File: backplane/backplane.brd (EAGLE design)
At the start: 177 x 80 mm, 9 parts, among them J1 09232486825, J2 09232486825, J3 09232486825, J4 09232486825, J5 09232486825, J6 09232486825, J7 09232486825, J8 09232486825, J9 TB009-508-04BE

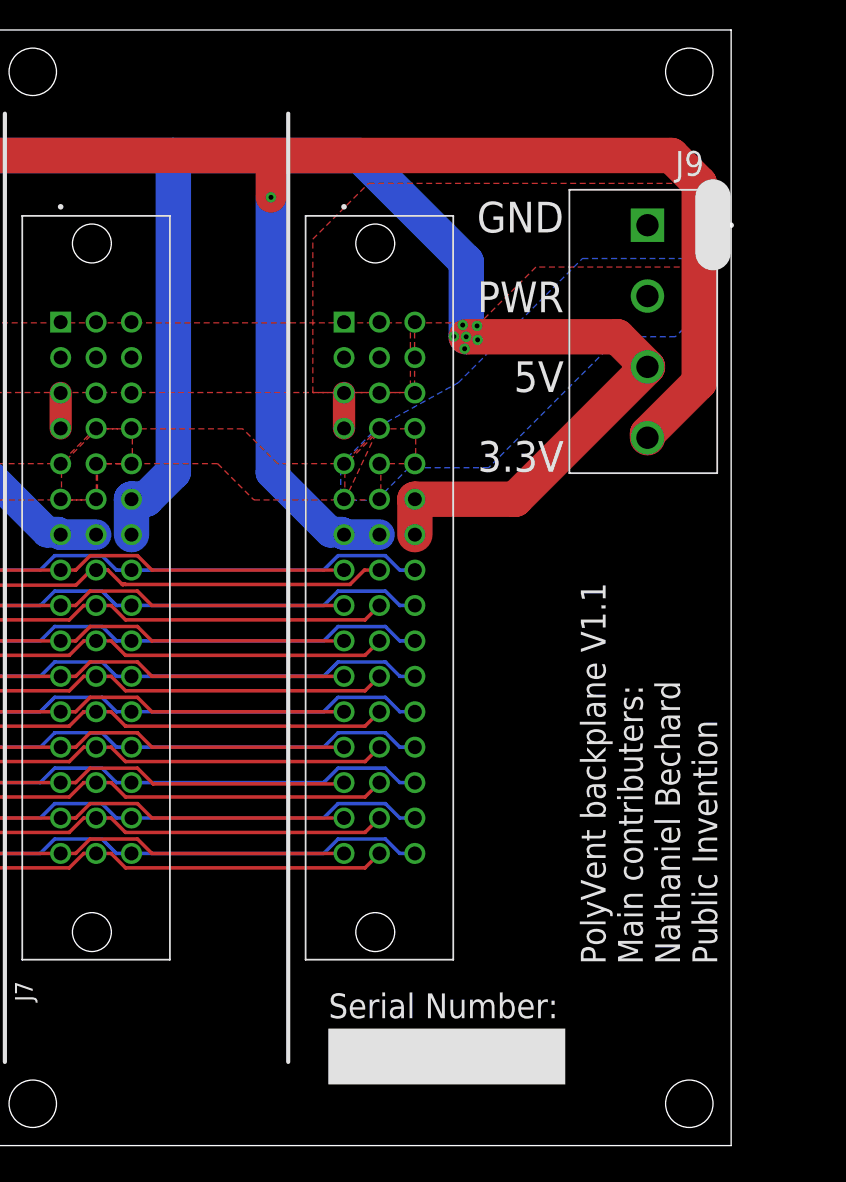
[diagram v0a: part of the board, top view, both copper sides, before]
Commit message: added labeled backplane breakout connector, backplane pcb is done
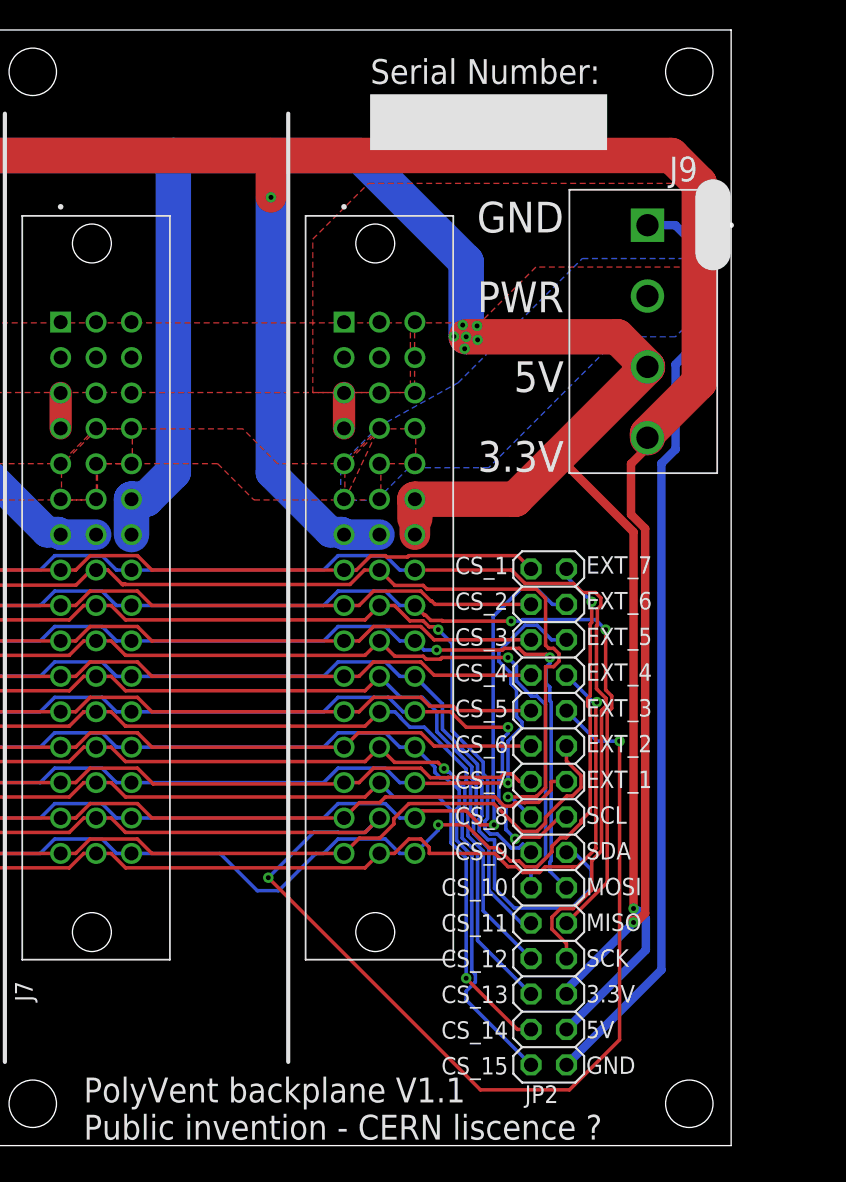
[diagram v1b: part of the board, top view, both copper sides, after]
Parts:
- added JP2: (no value), pinhead:2X15
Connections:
- removed net SS_1: J1.A8, J2.A8, J3.A8, J4.A8, J5.A8, J6.A8, J7.A8, J8.A8
- removed net SS_10: J1.B10, J2.B10, J3.B10, J4.B10, J5.B10, J6.B10, J7.B10, J8.B10
- removed net SS_11: J1.B11, J2.B11, J3.B11, J4.B11, J5.B11, J6.B11, J7.B11, J8.B11
- removed net SS_12: J1.B12, J2.B12, J3.B12, J4.B12, J5.B12, J6.B12, J7.B12, J8.B12
- removed net SS_13: J1.B13, J2.B13, J3.B13, J4.B13, J5.B13, J6.B13, J7.B13, J8.B13
- removed net SS_14: J1.B14, J2.B14, J3.B14, J4.B14, J5.B14, J6.B14, J7.B14, J8.B14
- removed net SS_15: J1.C13, J2.C13, J3.C13, J4.C13, J5.C13, J6.C13, J7.C13, J8.C13
- removed net SS_2: J1.A9, J2.A9, J3.A9, J4.A9, J5.A9, J6.A9, J7.A9, J8.A9
- removed net SS_3: J1.A10, J2.A10, J3.A10, J4.A10, J5.A10, J6.A10, J7.A10, J8.A10
- removed net SS_4: J1.A11, J2.A11, J3.A11, J4.A11, J5.A11, J6.A11, J7.A11, J8.A11
- removed net SS_5: J1.A12, J2.A12, J3.A12, J4.A12, J5.A12, J6.A12, J7.A12, J8.A12
- removed net SS_6: J1.A13, J2.A13, J3.A13, J4.A13, J5.A13, J6.A13, J7.A13, J8.A13
- removed net SS_7: J1.A14, J2.A14, J3.A14, J4.A14, J5.A14, J6.A14, J7.A14, J8.A14
- removed net SS_8: J1.B8, J2.B8, J3.B8, J4.B8, J5.B8, J6.B8, J7.B8, J8.B8
- removed net SS_9: J1.B9, J2.B9, J3.B9, J4.B9, J5.B9, J6.B9, J7.B9, J8.B9
- new net CS_1: J1.A8, J2.A8, J3.A8, J4.A8, J5.A8, J6.A8, J7.A8, J8.A8, JP2.30
- new net CS_10: J1.B10, J2.B10, J3.B10, J4.B10, J5.B10, J6.B10, J7.B10, J8.B10, JP2.12
- new net CS_11: J1.B11, J2.B11, J3.B11, J4.B11, J5.B11, J6.B11, J7.B11, J8.B11, JP2.10
- new net CS_12: J1.B12, J2.B12, J3.B12, J4.B12, J5.B12, J6.B12, J7.B12, J8.B12, JP2.8
- new net CS_13: J1.B13, J2.B13, J3.B13, J4.B13, J5.B13, J6.B13, J7.B13, J8.B13, JP2.6
- new net CS_14: J1.B14, J2.B14, J3.B14, J4.B14, J5.B14, J6.B14, J7.B14, J8.B14, JP2.4
- new net CS_15: J1.C13, J2.C13, J3.C13, J4.C13, J5.C13, J6.C13, J7.C13, J8.C13, JP2.2
- new net CS_2: J1.A9, J2.A9, J3.A9, J4.A9, J5.A9, J6.A9, J7.A9, J8.A9, JP2.28
- new net CS_3: J1.A10, J2.A10, J3.A10, J4.A10, J5.A10, J6.A10, J7.A10, J8.A10, JP2.26
- new net CS_4: J1.A11, J2.A11, J3.A11, J4.A11, J5.A11, J6.A11, J7.A11, J8.A11, JP2.24
- new net CS_5: J1.A12, J2.A12, J3.A12, J4.A12, J5.A12, J6.A12, J7.A12, J8.A12, JP2.22
- new net CS_6: J1.A13, J2.A13, J3.A13, J4.A13, J5.A13, J6.A13, J7.A13, J8.A13, JP2.20
- new net CS_7: J1.A14, J2.A14, J3.A14, J4.A14, J5.A14, J6.A14, J7.A14, J8.A14, JP2.18
- new net CS_8: J1.B8, J2.B8, J3.B8, J4.B8, J5.B8, J6.B8, J7.B8, J8.B8, JP2.16
- new net CS_9: J1.B9, J2.B9, J3.B9, J4.B9, J5.B9, J6.B9, J7.B9, J8.B9, JP2.14
- net 3.3V: now also JP2.5
- net 5V: now also JP2.3
- net EXT_1: now also JP2.17
- net EXT_2: now also JP2.19
- net EXT_3: now also JP2.21
- net EXT_4: now also JP2.23
- net EXT_5: now also JP2.25
- net EXT_6: now also JP2.27
- net EXT_7: now also JP2.29
- net GND: now also JP2.1
- net MISO: now also JP2.9
- net MOSI: now also JP2.11
- net SCK: now also JP2.7
- net SCL: now also JP2.15
- net SDA: now also JP2.13
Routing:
- net CS_8: track 0.00 -> 181.4 mm, vias 0 -> 1
- net CS_10: track 0.00 -> 176.3 mm, vias 0 -> 1
- net CS_15: track 0.00 -> 175.4 mm
- net CS_9: track 0.00 -> 173.2 mm, vias 0 -> 1
- net CS_14: track 0.00 -> 172.9 mm, vias 0 -> 1
- net CS_13: track 0.00 -> 172.5 mm, vias 0 -> 1
- net CS_11: track 0.00 -> 171.9 mm
- net CS_12: track 0.00 -> 171.8 mm
- net CS_7: track 0.00 -> 162.8 mm
- net CS_1: track 0.00 -> 162.7 mm
- net CS_2: track 0.00 -> 162.5 mm
- net CS_6: track 0.00 -> 162.5 mm
- net CS_5: track 0.00 -> 162.5 mm
- net CS_4: track 0.00 -> 162.5 mm
- net CS_3: track 0.00 -> 162.5 mm
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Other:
- board text added: "CS_1 CS_2 CS_3 CS_4 CS_5 CS_6 CS_7 CS_8 CS_9 CS_10 CS_11 CS_12 CS_13 CS_14 CS_15"
- board text added: "EXT_7 EXT_6 EXT_5 EXT_4 EXT_3 EXT_2 EXT_1 SCL SDA MOSI MISO SCK 3.3V 5V GND"
- board text added: "PolyVent backplane V1.1 Public invention - CERN liscence ?"
- board text removed: "PolyVent backplane V1.1 Main contributers: Nathaniel Bechard Public Invention"

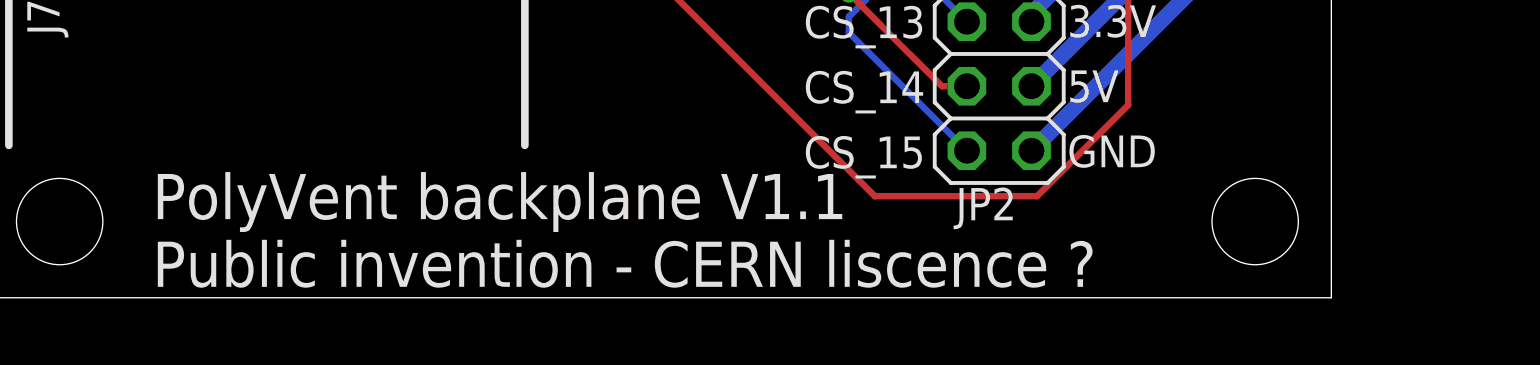
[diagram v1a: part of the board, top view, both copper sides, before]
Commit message: improved silkscreen for valve board
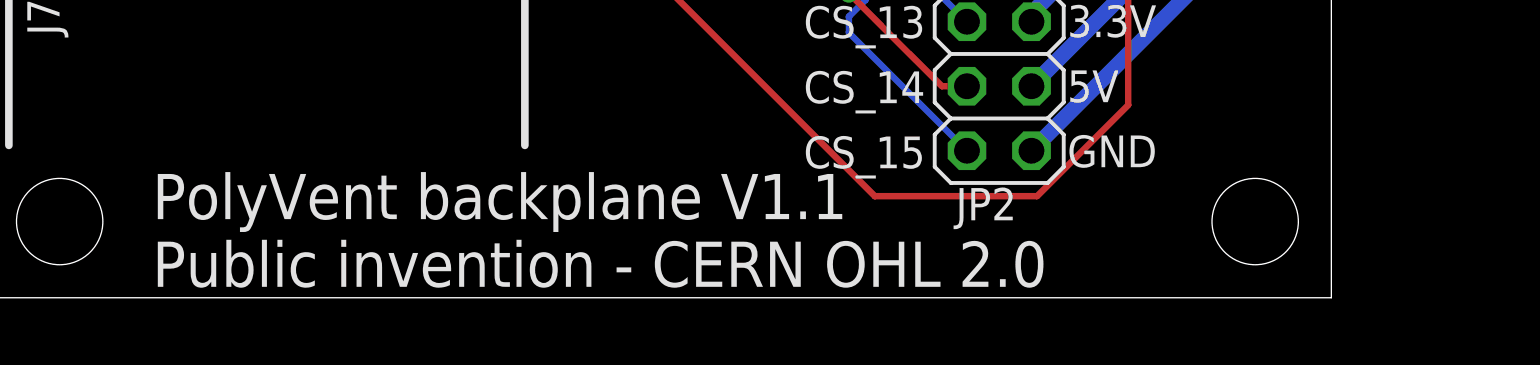
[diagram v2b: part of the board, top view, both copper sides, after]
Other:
- board text added: "PolyVent backplane V1.1 Public invention - CERN OHL 2.0"
- board text removed: "PolyVent backplane V1.1 Public invention - CERN liscence ?"
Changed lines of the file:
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@@
 <wire x1="175.7" y1="68.03" x2="175.7" y2="64.03" width="2.54" layer="25"/>
 <text x="130.57" y="0.43" size="1.778" layer="25">PolyVent backplane V1.1
-Public invention - CERN liscence ?</text>
+Public invention - CERN OHL 2.0</text>
 <rectangle x1="157.61" y1="64.89" x2="161.61" y2="81.89" layer="25" rot="R90"/>
 <text x="167.6" y="77.91" size="1.778" layer="25" rot="R180">Serial Number:</text>

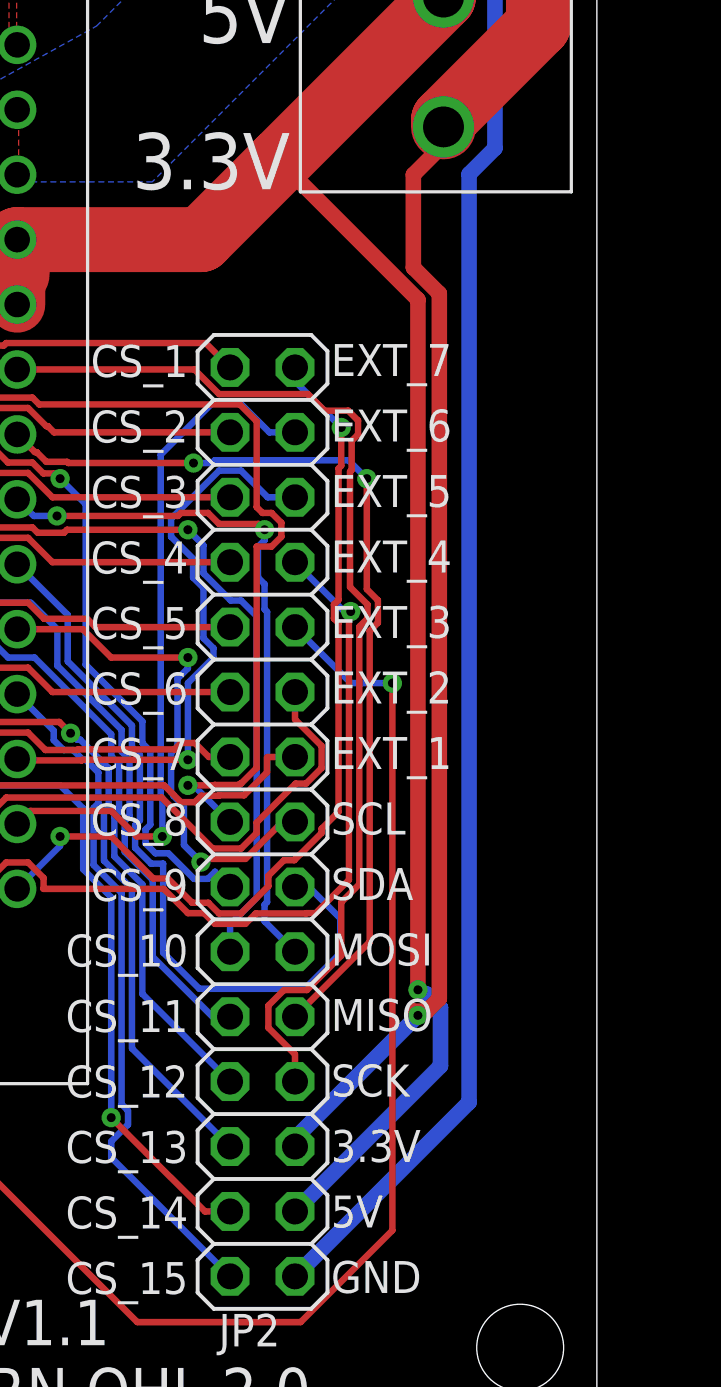
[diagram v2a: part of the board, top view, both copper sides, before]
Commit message: added a library for the switch I'll be using, and I updated the backplane pinout
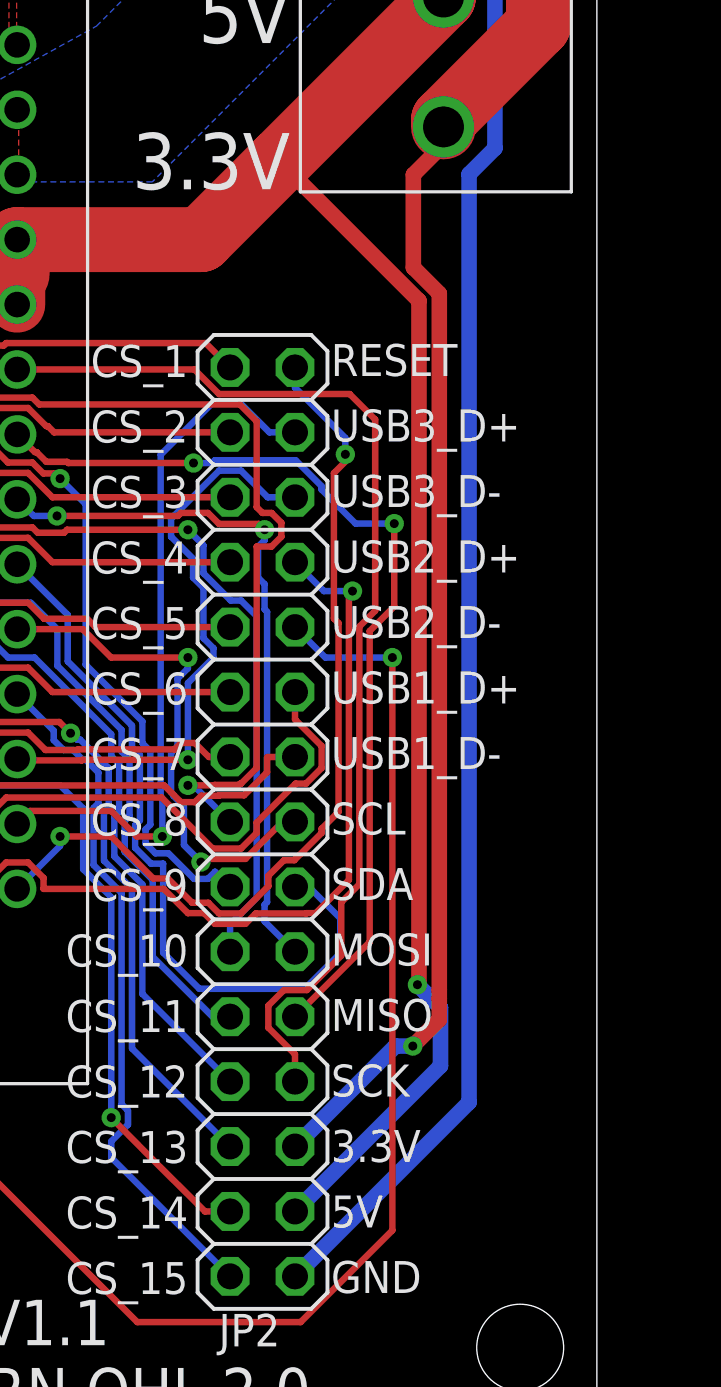
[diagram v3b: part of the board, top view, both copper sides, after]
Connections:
- net EXT_1 renamed USB1_D-
- net EXT_2 renamed USB1_D+
- net EXT_3 renamed USB2_D-
- net EXT_4 renamed USB2_D+
- net EXT_5 renamed USB3_D-
- net EXT_6 renamed USB3_D+
- net EXT_7 renamed RESET
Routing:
- net USB2_D+: track 179.7 -> 180.3 mm
- net USB2_D-: track 217.1 -> 217.7 mm
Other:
- board text added: "RESET USB3_D+ USB3_D- USB2_D+ USB2_D- USB1_D+ USB1_D- SCL SDA MOSI MISO SCK 3.3V 5V GND"
- board text removed: "EXT_7 EXT_6 EXT_5 EXT_4 EXT_3 EXT_2 EXT_1 SCL SDA MOSI MISO SCK 3.3V 5V GND"

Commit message: did some small correction work on the boards
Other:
- board text added: "PWR = 12V-24V"
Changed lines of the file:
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@@
 <grid distance="1" unitdist="mm" unit="mm" style="lines" multiple="1" display="no" altdistance="0.01" altunitdist="mm" altunit="mm"/>
 <layers>
-<layer number="1" name="Top" color="4" fill="1" visible="yes" active="yes"/>
+<layer number="1" name="Top" color="4" fill="1" visible="no" active="yes"/>
 <layer number="2" name="Route2" color="16" fill="1" visible="no" active="no"/>
 <layer number="3" name="Route3" color="17" fill="1" visible="no" active="no"/>
@@
 <layer number="14" name="Route14" color="22" fill="1" visible="no" active="no"/>
 <layer number="15" name="Route15" color="23" fill="1" visible="no" active="no"/>
-<layer number="16" name="Bottom" color="1" fill="1" visible="yes" active="yes"/>
+<layer number="16" name="Bottom" color="1" fill="1" visible="no" active="yes"/>
 <layer number="17" name="Pads" color="2" fill="1" visible="yes" active="yes"/>
 <layer number="18" name="Vias" color="2" fill="1" visible="yes" active="yes"/>
@@
 5V
 GND</text>
+<text x="158.38" y="44.01" size="1.8" layer="25">PWR = 12V-24V</text>
 </plain>
 <attributes>
